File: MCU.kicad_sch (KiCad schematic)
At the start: 26 parts, among them Q1 Q_NPN_BEC, U2 nRF51x22-QFxx, Y1 32.768kHz, Y2 16MHz

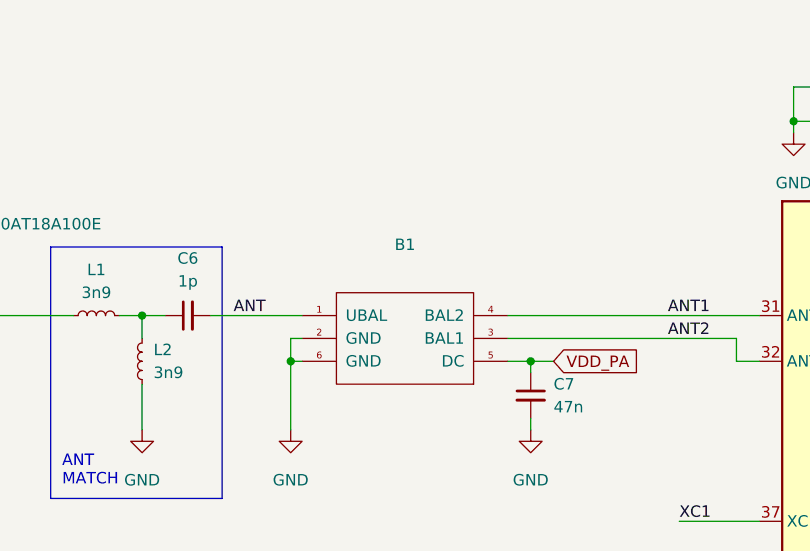
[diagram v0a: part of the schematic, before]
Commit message: feat: Assign LCSC ids to the schematic
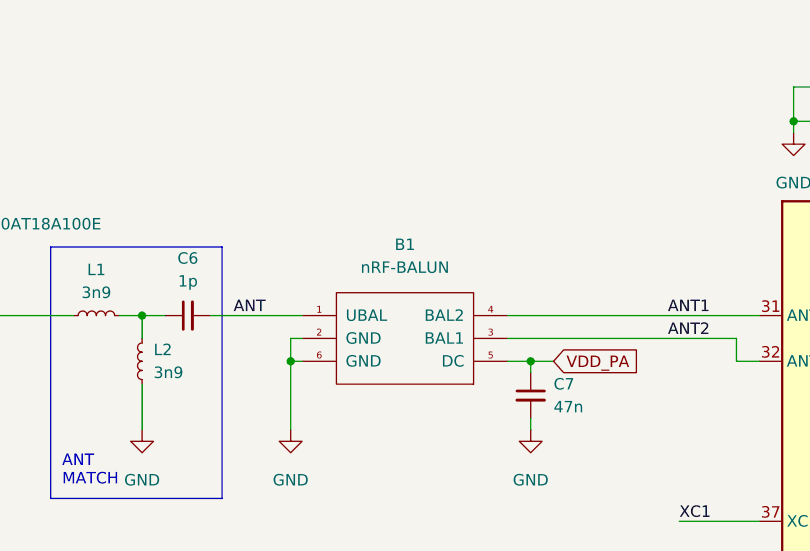
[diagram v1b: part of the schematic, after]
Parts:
- AE1: LCSC (none) -> C89334
- B1: value (none) -> nRF-BALUN; Mouser (none) -> 609-2450BM14E0003T
- C10, C11, C8, C9: LCSC (none) -> C106201
- C12, C13, C5: LCSC (none) -> C41851
- C14: LCSC (none) -> C575438
- C4, C7: LCSC (none) -> C5185458
- C6: LCSC (none) -> C710646
- L1, L2: LCSC (none) -> C961331
- Q1: LCSC (none) -> C553063
- R3: LCSC (none) -> C2906899
- R6: LCSC (none) -> C25940
- U2: LCSC (none) -> C167636
- Y1: LCSC (none) -> C32346
- Y2: LCSC (none) -> C362342
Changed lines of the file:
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@@
+      (effects (font (size 1.27 1.27)) hide)
+    )
+    (property "LCSC" "C41851" (id 4) (at 134.62 39.37 90)
       (effects (font (size 1.27 1.27)) hide)
     )
@@
       (effects (font (size 1.27 1.27)) hide)
     )
+    (property "LCSC" "C5185458" (id 4) (at 99.06 69.85 0)
+      (effects (font (size 1.27 1.27)) hide)
+    )
     (pin "1")
     (pin "2")
@@
     )
     (property "Datasheet" "~" (id 3) (at 231.14 45.72 0)
+      (effects (font (size 1.27 1.27)) hide)
+    )
+    (property "LCSC" "C41851" (id 4) (at 231.14 45.72 0)
       (effects (font (size 1.27 1.27)) hide)
     )
@@
       (effects (font (size 1.27 1.27)) hide)
     )
+    (property "LCSC" "C2906899" (id 4) (at 223.52 91.44 90)
+      (effects (font (size 1.27 1.27)) hide)
+    )
     (pin "1")
     (pin "2")
@@
       (effects (font (size 1.27 1.27)) hide)
     )
+    (property "LCSC" "C106201" (id 4) (at 69.85 139.7 90)
+      (effects (font (size 1.27 1.27)) hide)
+    )
     (pin "1")
     (pin "2")
@@
       (effects (font (size 1.27 1.27)) hide)
     )
+    (property "LCSC" "C575438" (id 4) (at 242.57 45.72 0)
+      (effects (font (size 1.27 1.27)) hide)
+    )
     (pin "1")
     (pin "2")
@@
     )
     (property "Datasheet" "~" (id 3) (at 218.44 45.72 0)
+      (effects (font (size 1.27 1.27)) hide)
+    )
+    (property "LCSC" "C41851" (id 4) (at 218.44 45.72 0)
       (effects (font (size 1.27 1.27)) hide)
     )
@@
       (effects (font (size 1.27 1.27)) hide)
     )
+    (property "LCSC" "C5185458" (id 4) (at 134.62 35.56 90)
+      (effects (font (size 1.27 1.27)) hide)
+    )
     (pin "1")
     (pin "2")
@@
       (effects (font (size 1.27 1.27)) hide)
     )
+    (property "LCSC" "C106201" (id 4) (at 69.85 154.94 90)
+      (effects (font (size 1.27 1.27)) hide)
+    )
     (pin "1")
     (pin "2")
@@
     (in_bom yes) (on_board yes) (fields_autoplaced)
     (property "Reference" "B1" (id 0) (at 85.09 53.086 0))
-    (property "Value" "" (id 1) (at 85.09 55.626 0))
+    (property "Value" "nRF-BALUN" (id 1) (at 85.09 55.626 0))
     (property "Footprint" "Library:FIL_2450BM14E0003T" (id 2) (at 85.09 69.85 0)
       (effects (font (size 1.27 1.27)) hide)
     )
     (property "Datasheet" "DOCUMENTATION" (id 3) (at 85.09 72.39 0)
+      (effects (font (size 1.27 1.27)) hide)
+    )
+    (property "Mouser" "609-2450BM14E0003T" (id 4) (at 85.09 63.5 0)
       (effects (font (size 1.27 1.27)) hide)
     )
@@
       (effects (font (size 1.27 1.27)) hide)
     )
+    (property "LCSC" "C89334" (id 4) (at 38.1 55.88 0)
+      (effects (font (size 1.27 1.27)) hide)
+    )
     (pin "1")
   )
@@
       (effects (font (size 1.27 1.27)) hide)
     )
+    (property "LCSC" "C961331" (id 4) (at 55.88 66.04 0)
+      (effects (font (size 1.27 1.27)) hide)
+    )
     (pin "1")
     (pin "2")
@@
     )
     (property "Datasheet" "http://infocenter.nordicsemi.com/pdf/nRF51822_PS_v3.3.pdf" (id 3) (at 137.16 93.98 0)
+      (effects (font (size 1.27 1.27)) hide)
+    )
+    (property "LCSC" "C167636" (id 4) (at 147.32 91.44 0)
       (effects (font (size 1.27 1.27)) hide)
     )
@@
       (effects (font (size 1.27 1.27)) hide)
     )
+    (property "LCSC" "C25940" (id 4) (at 179.07 92.71 0)
+      (effects (font (size 1.27 1.27)) hide)
+    )
     (pin "1")
     (pin "2")
@@
       (effects (font (size 1.27 1.27)) hide)
     )
+    (property "LCSC" "C710646" (id 4) (at 60.96 60.96 90)
+      (effects (font (size 1.27 1.27)) hide)
+    )
     (pin "1")
     (pin "2")
@@
       (effects (font (size 1.27 1.27)) hide)
     )
+    (property "LCSC" "C961331" (id 4) (at 50.8 60.96 90)
+      (effects (font (size 1.27 1.27)) hide)
+    )
     (pin "1")
     (pin "2")
@@
     )
     (property "Datasheet" "~" (id 3) (at 76.2 147.32 0)
+      (effects (font (size 1.27 1.27)) hide)
+    )
+    (property "LCSC" "C32346" (id 4) (at 76.2 147.32 90)
       (effects (font (size 1.27 1.27)) hide)
     )
@@
       (effects (font (size 1.27 1.27)) hide)
     )
+    (property "LCSC" "C106201" (id 4) (at 68.58 96.52 90)
+      (effects (font (size 1.27 1.27)) hide)
+    )
     (pin "1")
     (pin "2")
@@
     )
     (property "Datasheet" "~" (id 3) (at 233.68 91.44 0)
+      (effects (font (size 1.27 1.27)) hide)
+    )
+    (property "LCSC" "C553063" (id 4) (at 233.68 91.44 0)
       (effects (font (size 1.27 1.27)) hide)
     )
@@
       (effects (font (size 1.27 1.27)) hide)
     )
+    (property "LCSC" "C106201" (id 4) (at 68.58 111.76 90)
+      (effects (font (size 1.27 1.27)) hide)
+    )
     (pin "1")
     (pin "2")
@@
       (effects (font (size 1.27 1.27)) hide)
     )
+    (property "LCSC" "C362342" (id 4) (at 74.93 104.14 90)
+      (effects (font (size 1.27 1.27)) hide)
+    )

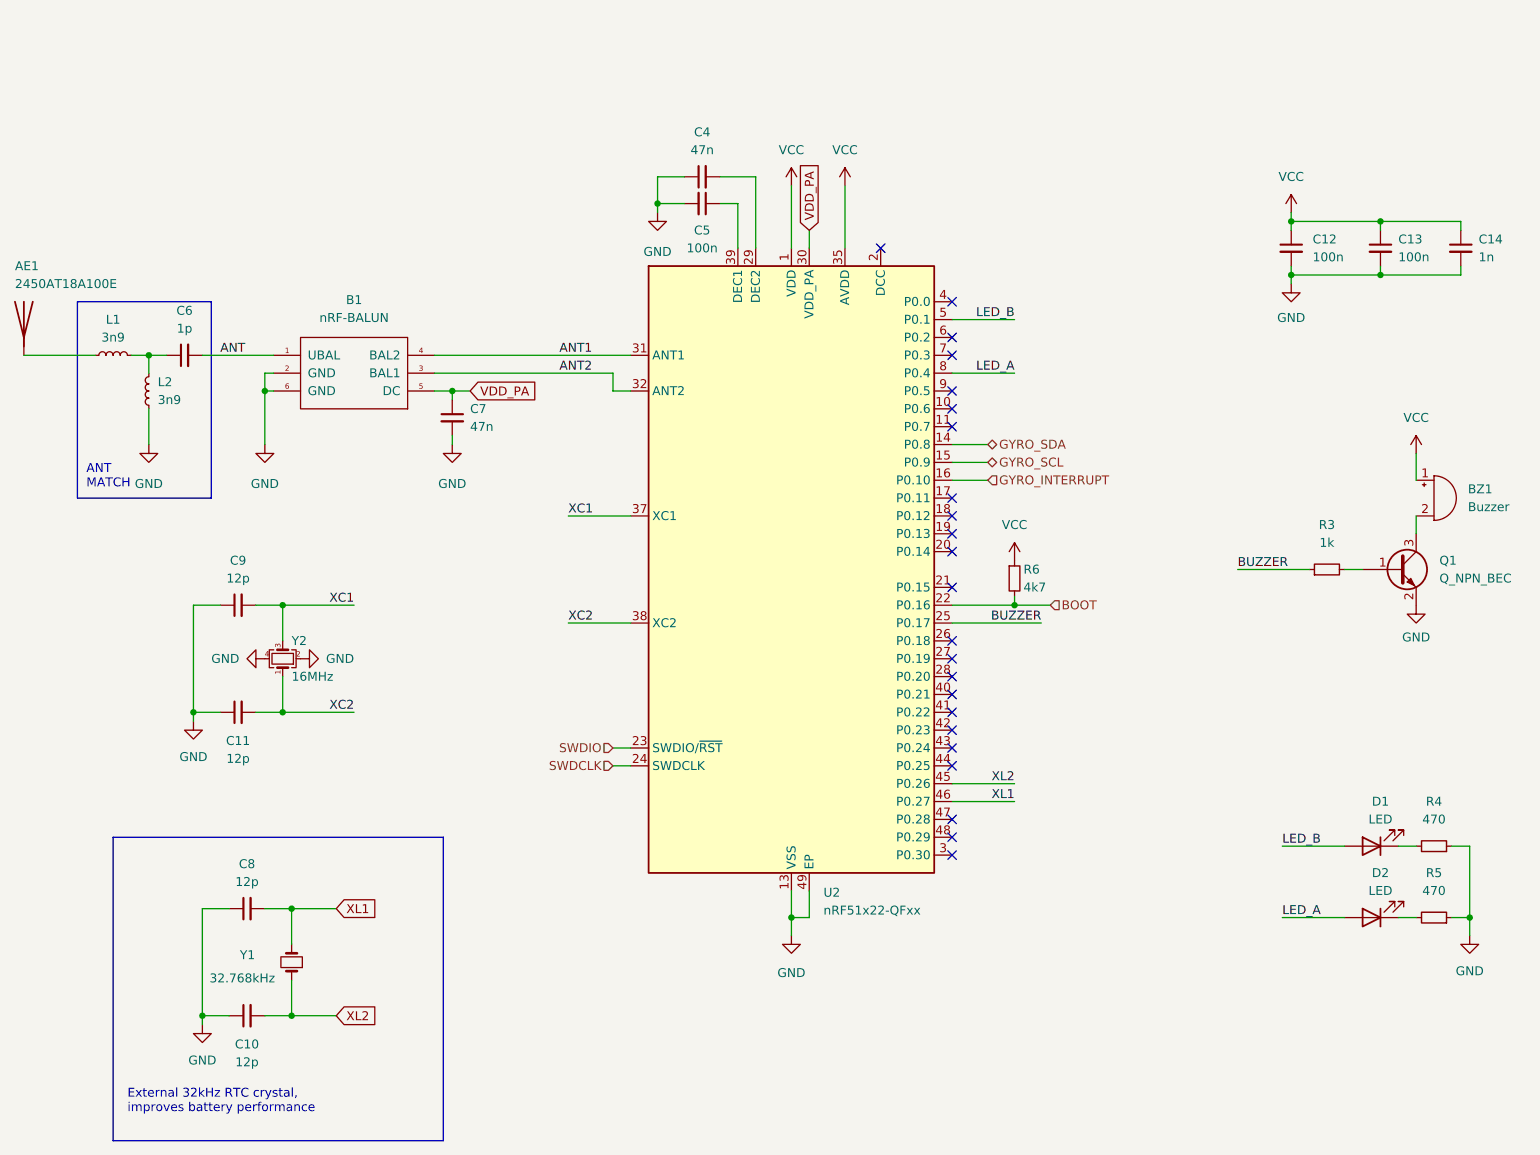
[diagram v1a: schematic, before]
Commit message: Change schematic to NRF52832
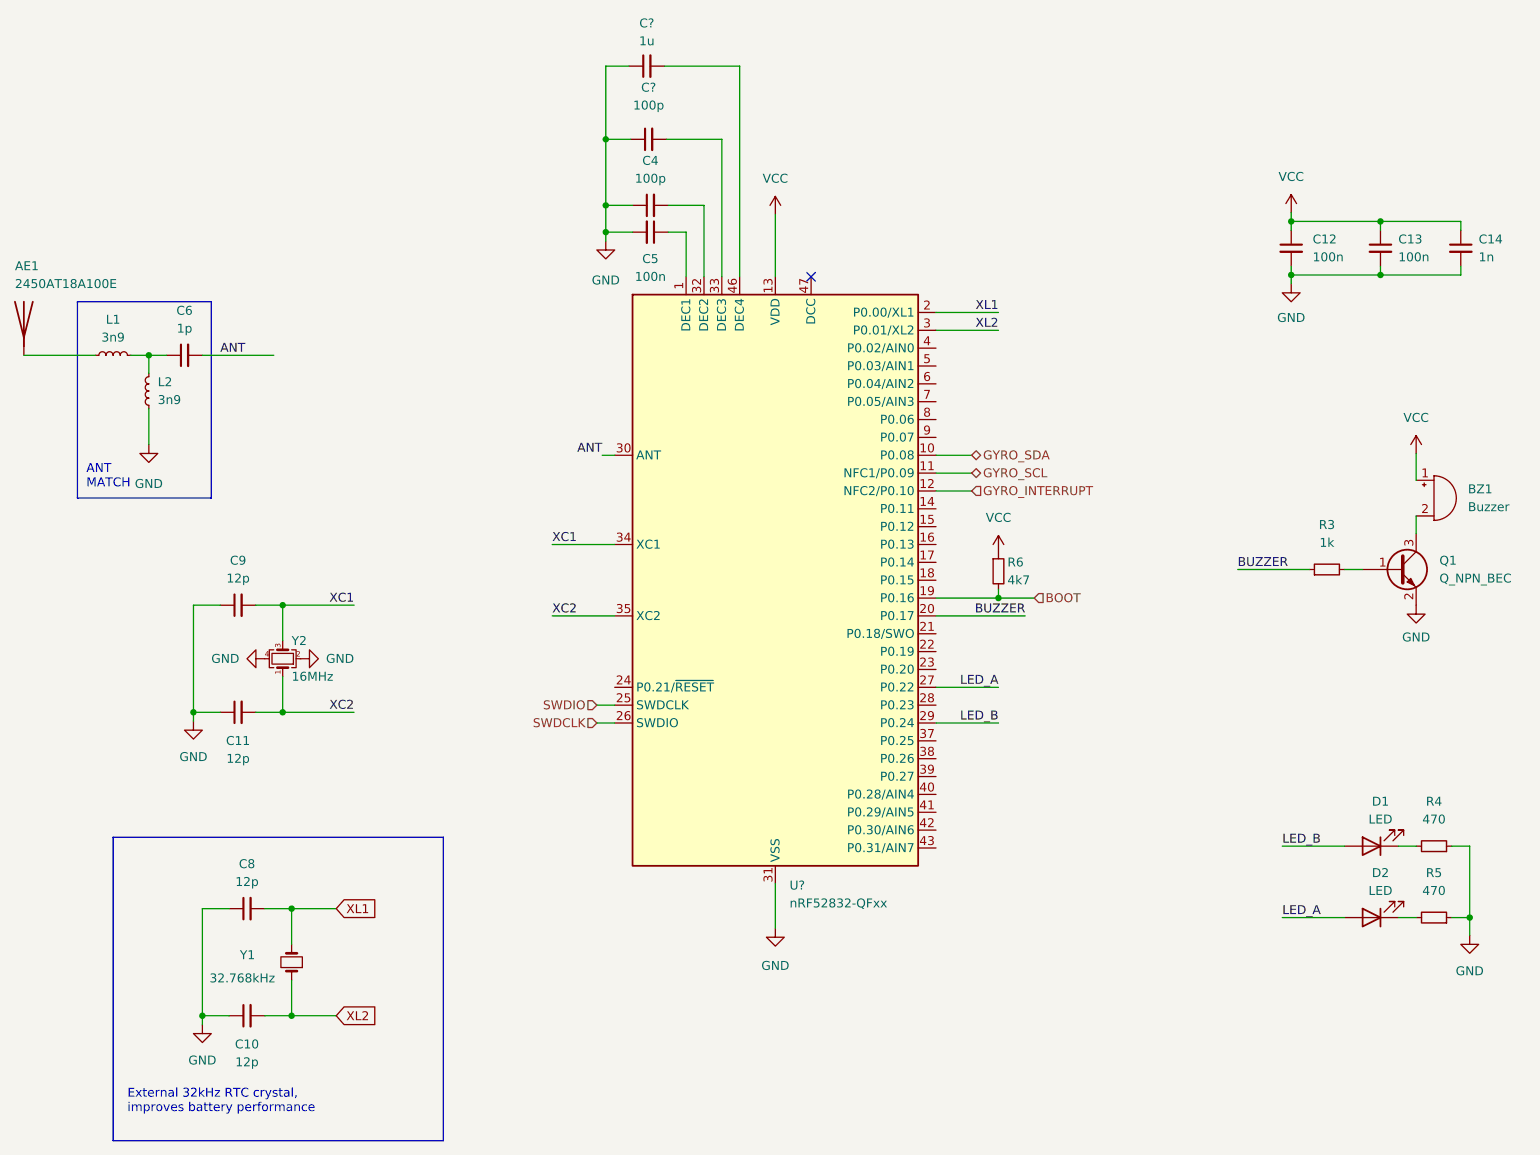
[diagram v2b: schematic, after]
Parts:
- removed B1: nRF-BALUN, Library:FIL_2450BM14E0003T, symbol Lib:nRF-BALUN
- removed C7: 47n, Capacitor_SMD:C_0402_1005Metric, symbol Device:C_Small
- removed U2: nRF51x22-QFxx, Package_DFN_QFN:QFN-48-1EP_6x6mm_P0.4mm_EP4.6x4.6mm, symbol MCU_Nordic:nRF51x22-QFxx
- added C?: 1u, Capacitor_SMD:C_0402_1005Metric, symbol Device:C_Small
- added C?: 100p, Capacitor_SMD:C_0402_1005Metric, symbol Device:C_Small
- added U?: nRF52832-QFxx, Package_DFN_QFN:QFN-48-1EP_6x6mm_P0.4mm_EP4.6x4.6mm, symbol MCU_Nordic:nRF52832-QFxx
- C4: value 47n -> 100p; LCSC C5185458 -> (none)
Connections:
- net ANT: now also U?.30 (ANT)
- net BOOT: now also U?.19 (P0.16)
- net BUZZER: now also U?.20 (P0.17)
- net GND: now also C?.1, C?.1, U?.31 (VSS), U?.45 (VSS), U?.49 (VSS)
- net GYRO_INTERRUPT: now also U?.12 (NFC2/P0.10)
- net GYRO_SCL: now also U?.11 (NFC1/P0.09)
- net GYRO_SDA: now also U?.10 (P0.08)
- net LED_A: now also U?.27 (P0.22)
- net LED_B: now also U?.29 (P0.24)
- net SWDCLK: now also U?.26 (SWDIO)
- net SWDIO: now also U?.25 (SWDCLK)
- net VCC: now also U?.13 (VDD), U?.36 (VDD), U?.48 (VDD)
- net XC1: now also U?.34 (XC1)
- net XC2: now also U?.35 (XC2)
- net XL1: now also U?.2 (P0.00/XL1)
- net XL2: now also U?.3 (P0.01/XL2)
- net at C5.1: now also U?.1 (DEC1)
- net at C4.2: now also U?.32 (DEC2)
- new net: C?.2, U?.46 (DEC4)
- new net: C?.2, U?.33 (DEC3)
- no-connect marks 23 -> 1
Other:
- moved on the sheet: C4, C5, R6
